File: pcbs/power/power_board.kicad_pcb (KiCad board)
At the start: 2 copper layers, 114 x 137.6 mm, 62 parts, among them J10 MR30PW-M, J11 MR30PW-M, J12 12V connection, J4 JST_XH_B3B, J5 JST_XH_B3B, J6 XT30PW-F, J7 XT30PW-F, J8 XT30PW-M, J9 MR30PW-M, U1 TPS5430DDA, U2 TPS5430DDA, U4 TPS5430DDA

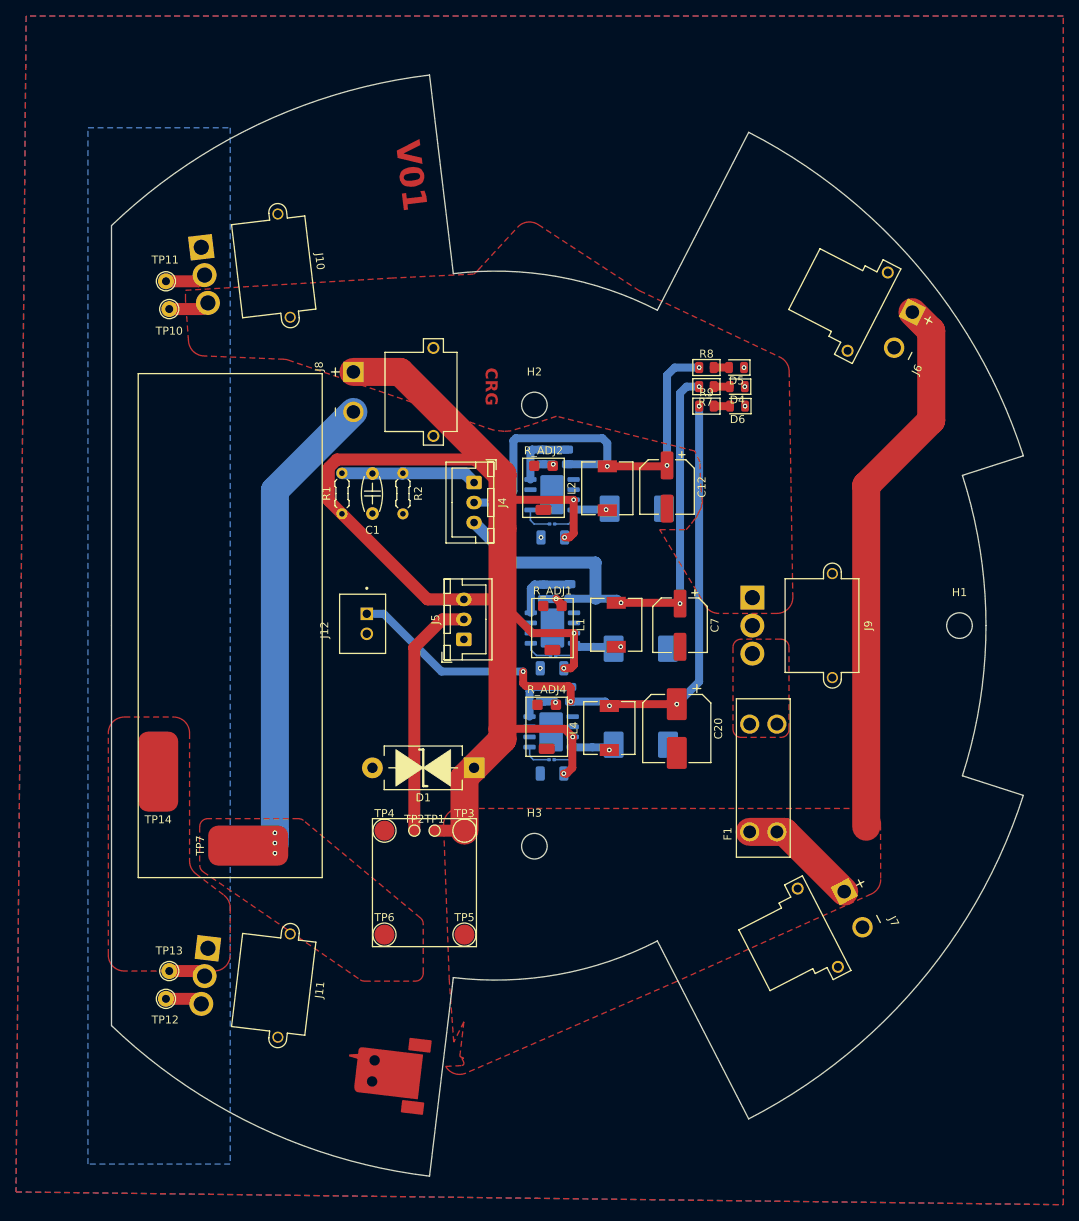
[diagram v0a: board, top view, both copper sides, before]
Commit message: Atualização para versão 10.0 do kicad Condensação do Layout Mudança no circuito V_mon para diminuir impedância de saída Implementação de Circuito "E-Switch" low side Resolução de EDR's no esquemático e PCB
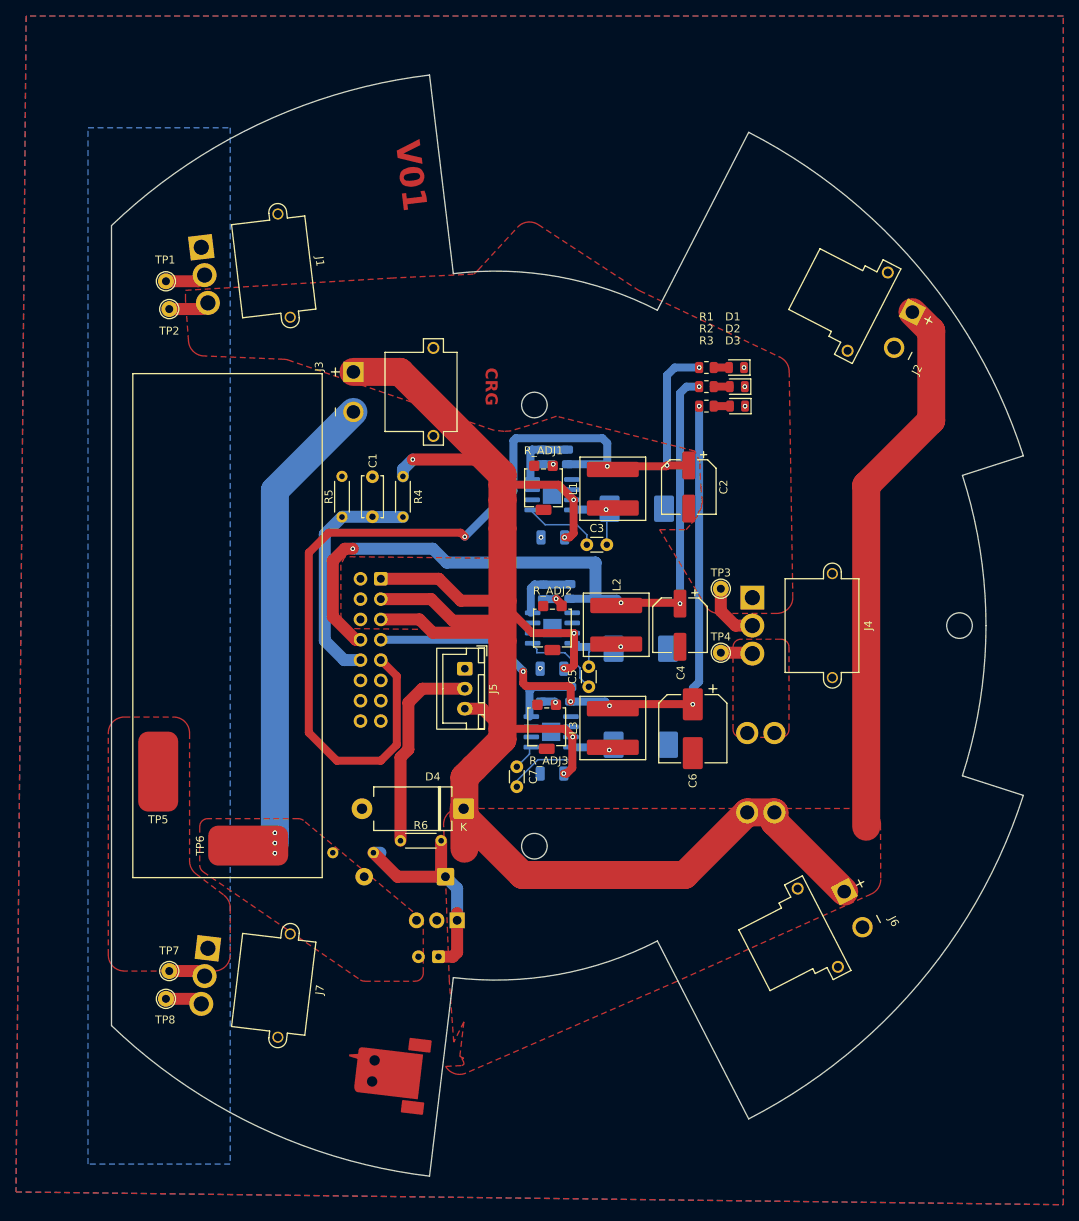
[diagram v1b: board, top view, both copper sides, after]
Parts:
- removed the C4 at (96.1, 91.4)
- removed the C6 at (96.2, 107.8)
- removed J12: 12V connection, oxebots_connectors:JST_B2B-XH-A
- removed the J4 at (86.3, 86.2)
- removed the TP1 at (81.4, 129.7)
- removed the TP2 at (78.8, 129.7)
- removed the TP5 at (85.1, 142.7)
- removed the TP6 at (75.1, 142.7)
- added C11: 10uF, Capacitor_THT:CP_Radial_D5.0mm_P2.50mm, B.Cu at (81.9, 145.5)
- added C3: 0.01uF, Capacitor_THT:C_Disc_D3.0mm_W1.6mm_P2.50mm, F.Cu at (100.4, 94.0)
- added C7: 0.01uF, Capacitor_THT:C_Disc_D3.0mm_W1.6mm_P2.50mm, F.Cu at (91.7, 121.7)
- added D8: 1N4744A, Diode_THT:D_DO-41_SOD81_P10.16mm_Horizontal, B.Cu at (82.7, 135.5)
- added J8: Conn_02x08_Odd_Even, Connector_IDC:IDC-Header_2x08_P2.54mm_Vertical, B.Cu at (74.7, 98.2)
- added Q1: IRFB3205, Package_TO_SOT_THT:TO-220-3_Vertical, B.Cu at (84.2, 140.9)
- added R13: 100K, Resistor_THT:R_Axial_DIN0204_L3.6mm_D1.6mm_P5.08mm_Horizontal, B.Cu at (73.7, 132.5)
- added R6: 10k, Resistor_THT:R_Axial_DIN0204_L3.6mm_D1.6mm_P5.08mm_Horizontal, F.Cu at (77.1, 131.0)
- C1: footprint PCM_Capacitor_THT_AKL:C_Disc_D5.0mm_W2.5mm_P5.00mm -> Capacitor_THT:C_Disc_D5.0mm_W2.5mm_P5.00mm
- C5: footprint Capacitor_SMD:C_0201_0603Metric -> Capacitor_THT:C_Disc_D3.0mm_W1.6mm_P2.50mm; moved to F.Cu
- D4: renamed from D1; footprint PCM_Diode_THT_AKL:D_DO-201_P12.70mm_Horizontal_TVS -> Diode_THT:D_DO-201_P12.70mm_Horizontal
- F1: value 30A -> 30; footprint oxebots:FUSE_3557-10 -> Fuse:Fuseholder_Blade_Mini_Keystone_3568; moved to B.Cu
- J1: renamed from J10; footprint oxebots_connectors:AMASS_MR30PW-M_1x03_P3.50mm_Horizontal -> oxebots:AMASS_MR30PW-M_1x03_P3.50mm_Horizontal
- J2: renamed from J6; footprint oxebots_connectors:AMASS_XT30PW-F -> oxebots:AMASS_XT30PW-F
- J3: renamed from J8; footprint oxebots_connectors:AMASS_XT30PW-M -> oxebots:AMASS_XT30PW-M
- J4: renamed from J9; footprint oxebots_connectors:AMASS_MR30PW-M_1x03_P3.50mm_Horizontal -> oxebots:AMASS_MR30PW-M_1x03_P3.50mm_Horizontal
- J6: renamed from J7; footprint oxebots_connectors:AMASS_XT30PW-F -> oxebots:AMASS_XT30PW-F
- J7: renamed from J11; footprint oxebots_connectors:AMASS_MR30PW-M_1x03_P3.50mm_Horizontal -> oxebots:AMASS_MR30PW-M_1x03_P3.50mm_Horizontal
- L1: renamed from L2; footprint Inductor_SMD:L_6.3x6.3_H3 -> Inductor_SMD:L_Coilcraft_XAL7070-XXX
- L2: renamed from L1; footprint Inductor_SMD:L_6.3x6.3_H3 -> Inductor_SMD:L_Coilcraft_XAL7070-XXX
- L3: renamed from L4; footprint Inductor_SMD:L_6.3x6.3_H3 -> Inductor_SMD:L_Coilcraft_XAL7070-XXX
- R1: renamed from R8; footprint PCM_Resistor_SMD_AKL:R_0805_2012Metric -> Resistor_SMD:R_0805_2012Metric
- R10: renamed from R4; footprint PCM_Resistor_SMD_AKL:R_0805_2012Metric -> Resistor_SMD:R_0805_2012Metric
- R11: renamed from R16; footprint PCM_Resistor_SMD_AKL:R_0805_2012Metric -> Resistor_SMD:R_0805_2012Metric
- R12: renamed from R15; footprint PCM_Resistor_SMD_AKL:R_0805_2012Metric -> Resistor_SMD:R_0805_2012Metric
- R2: renamed from R7; footprint PCM_Resistor_SMD_AKL:R_0805_2012Metric -> Resistor_SMD:R_0805_2012Metric
- R3: renamed from R9; footprint PCM_Resistor_SMD_AKL:R_0805_2012Metric -> Resistor_SMD:R_0805_2012Metric
- R4: renamed from R1; value 5.6M -> 56K; footprint PCM_Resistor_THT_AKL:R_Axial_DIN0204_L3.6mm_D1.6mm_P5.08mm_Horizontal -> Resistor_THT:R_Axial_DIN0204_L3.6mm_D1.6mm_P5.08mm_Horizontal
- R5: renamed from R2; value 220K -> 2.2K; footprint PCM_Resistor_THT_AKL:R_Axial_DIN0204_L3.6mm_D1.6mm_P5.08mm_Horizontal -> Resistor_THT:R_Axial_DIN0204_L3.6mm_D1.6mm_P5.08mm_Horizontal
- R7: renamed from R6; footprint PCM_Resistor_SMD_AKL:R_0805_2012Metric -> Resistor_SMD:R_0805_2012Metric
- R8: renamed from R5; footprint PCM_Resistor_SMD_AKL:R_0805_2012Metric -> Resistor_SMD:R_0805_2012Metric
- R9: renamed from R3; footprint PCM_Resistor_SMD_AKL:R_0805_2012Metric -> Resistor_SMD:R_0805_2012Metric
- R_ADJ1: renamed from R_ADJ2; footprint PCM_Potentiometer_SMD_AKL:Potentiometer_Bourns_3314G_Vertical -> Potentiometer_SMD:Potentiometer_Bourns_3314G_Vertical
- R_ADJ2: renamed from R_ADJ1; footprint PCM_Potentiometer_SMD_AKL:Potentiometer_Bourns_3314G_Vertical -> Potentiometer_SMD:Potentiometer_Bourns_3314G_Vertical
- R_ADJ3: renamed from R_ADJ4; footprint PCM_Potentiometer_SMD_AKL:Potentiometer_Bourns_3314G_Vertical -> Potentiometer_SMD:Potentiometer_Bourns_3314G_Vertical
- TP3: value V+ -> B5; footprint TestPoint:TestPoint_Pad_D2.5mm -> TestPoint:TestPoint_THTPad_D2.0mm_Drill1.0mm
- TP4: value V^{-}_{no} -> B6; footprint TestPoint:TestPoint_Pad_D2.5mm -> TestPoint:TestPoint_THTPad_D2.0mm_Drill1.0mm
- U1: renamed from U2; footprint PCM_Package_SO_AKL:Texas_HSOP-8-1EP_3.9x4.9mm_P1.27mm -> Package_SO:HSOP-8-1EP_3.9x4.9mm_P1.27mm_EP2.3x2.3mm
- U2: renamed from U1; footprint PCM_Package_SO_AKL:Texas_HSOP-8-1EP_3.9x4.9mm_P1.27mm -> Package_SO:HSOP-8-1EP_3.9x4.9mm_P1.27mm_EP2.3x2.3mm
- U3: renamed from U4; footprint PCM_Package_SO_AKL:Texas_HSOP-8-1EP_3.9x4.9mm_P1.27mm -> Package_SO:HSOP-8-1EP_3.9x4.9mm_P1.27mm_EP2.3x2.3mm
- moved TP4 47.6 mm to (117.2, 107.5)
- moved TP3 44.1 mm to (117.2, 99.5)
- moved C5 10.2 mm to (100.7, 111.7), turned to 90 degrees
- moved R5 9.39 mm to (69.8, 90.5), turned to 90 degrees
- moved R4 8.94 mm to (77.4, 85.4), turned to -90 degrees
- moved F1 5.97 mm to (120.5, 117.5), turned to -90 degrees
- moved D4 5.27 mm to (85.0, 127.0)
- moved C1 4.60 mm to (73.6, 85.5), turned to -90 degrees
- moved J5 3.67 mm to (85.2, 109.5), turned to -90 degrees
- moved C2 2.72 mm to (113.2, 86.8)
- moved C6 2.00 mm to (113.7, 117.0)
- moved L1 0.69 mm to (103.7, 87.0)
- moved L3 0.44 mm to (103.7, 116.9)
- moved C9 0.06 mm to (96.1, 109.5)
- renumbered C3 to C10, C12 to C2, C7 to C4, C20 to C6, C2 to C8, C8 to C9, D5 to D1, D4 to D2, D6 to D3, D2 to D5, D7 to D6, D3 to D7, H2 to H1, H1 to H2, TP11 to TP1, TP10 to TP2, TP14 to TP5, TP7 to TP6, TP13 to TP7, TP12 to TP8
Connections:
- net /V_{MON} renamed VMon
- C5 pad 1: Net-(D3-K) -> Net-(U1-BOOT)
- C5 pad 2: Net-(U4-BOOT) -> Net-(D7-K)
- J5 pad 2: Net-(J5-Pin_2) -> SW_{NO}
- TP3 pad 1: V_{ BATT} -> Net-(J9-Pin_2)
- TP4 pad 1: GND -> /B_{6s}
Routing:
- net +3.3V: track 55.1 -> 128.7 mm, vias 3 -> 4
- net V_{ BATT}: track 260.0 -> 319.7 mm, vias 6 -> 7
- net Net-(J5-Pin_2): track 30.5 -> 0.00 mm
- net Net-(D9-K): track 0.00 -> 29.8 mm
- net +5V: track 64.9 -> 93.5 mm, vias 3 -> 4
- net SW_{NO}: track 0.00 -> 25.4 mm
- net VMon: track 17.0 -> 29.4 mm
- net Net-(J9-Pin_2): track 0.00 -> 7.49 mm
- net Net-(U1-BOOT): track 3.58 -> 10.5 mm
- net Net-(D3-K): track 8.38 -> 14.9 mm
- net Net-(U2-BOOT): track 3.88 -> 9.58 mm
- net /B_{6s}: track 0.00 -> 3.99 mm
- net +12V: track 83.9 -> 82.0 mm
- net Net-(D7-K): track 9.75 -> 8.83 mm
- net Net-(D2-K): track 7.83 -> 8.73 mm
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
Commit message: Versão final com inclusão de test_points
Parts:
- added TP10: 5V, TestPoint:TestPoint_THTPad_D2.0mm_Drill1.0mm, F.Cu at (106.7, 80.0)
- added TP11: 3.3V, TestPoint:TestPoint_THTPad_D2.0mm_Drill1.0mm, F.Cu at (106.7, 74.5)
- added TP12: V_MON, TestPoint:TestPoint_THTPad_D2.0mm_Drill1.0mm, F.Cu at (82.7, 88.5)
- added TP13: V_BAT, TestPoint:TestPoint_THTPad_D2.0mm_Drill1.0mm, B.Cu at (135.2, 90.5)
- added TP9: 12V, TestPoint:TestPoint_THTPad_D2.0mm_Drill1.0mm, F.Cu at (118.2, 81.0)
- renumbered C7 to C10, C5 to C4, C3 to C5, C11 to C8, D8 to D3, H2 to H1, H1 to H2, J8 to J1, J1 to J5, J7 to J6, J5 to J7, R4 to R1, R5 to R2, R13 to R5, R6 to R8, TP8 to TP2, TP7 to TP3, TP5 to TP4, TP4 to TP5, TP3 to TP6, TP2 to TP7, TP1 to TP8
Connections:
- C8 pad 1: Net-(D9-K) -> Net-(D3-K)
- D3 pad 1: Net-(D9-K) -> Net-(D3-K)
- Q1 pad 1: Net-(D9-K) -> Net-(D3-K)
- R5 pad 1: Net-(D9-K) -> Net-(D3-K)
- R8 pad 2: Net-(D9-K) -> Net-(D3-K)
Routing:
- net Net-(D3-K): track 14.9 -> 58.3 mm
- net Net-(D9-K): track 29.8 -> 0.00 mm
- net VMon: track 29.4 -> 36.1 mm
- net +5V: track 93.5 -> 99.1 mm, vias 4 -> 5
- net +3.3V: track 128.7 -> 133.1 mm
- net +12V: track 82.0 -> 85.9 mm
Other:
- board text added: "12V"
- board text added: "3V3"
- board text added: "5V"

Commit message: DRC warnings solving
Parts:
- removed the C10 at (96.1, 122.6)
- removed the C4 at (112.1, 104.0)
- removed the C6 at (113.7, 117.0)
- removed the D1 at (119.1, 71.8)
- removed the J6 at (129.3, 141.9)
- removed the R1 at (115.4, 71.8)
- removed the R2 at (115.4, 74.2)
- removed the R3 at (115.4, 76.7)
- removed the TP6 at (58.1, 131.6)
- removed the TP6 at (117.2, 99.5)
- added C11: 220uF, Capacitor_SMD:CP_Elec_8x6.2, F.Cu at (113.7, 116.9)
- added C3: 100nF, Capacitor_THT:C_Disc_D3.0mm_W1.6mm_P2.50mm, F.Cu at (73.7, 90.5)
- added C7: 220uF, Capacitor_SMD:CP_Elec_6.3x7.7, F.Cu at (112.1, 104.0)
- added D8: B340, Diode_SMD:D_SMC, B.Cu at (107.2, 119.0)
- added R13: 10k, Resistor_SMD:R_0805_2012Metric, B.Cu at (98.2, 112.7)
- added R4: 2.7k, Resistor_SMD:R_0805_2012Metric, B.Cu at (95.0, 99.9)
- added R5: 5.6k, Resistor_SMD:R_0805_2012Metric, B.Cu at (95.2, 83.0)
- added TP15: P-, Connector_Wire:SolderWirePad_1x01_SMD_5x10mm, F.Cu at (57.9, 130.7)
- added TP6: B5, TestPoint:TestPoint_THTPad_D2.0mm_Drill1.0mm, F.Cu at (116.9, 98.2)
- C1: value 100nF -> 10uF; footprint Capacitor_THT:C_Disc_D5.0mm_W2.5mm_P5.00mm -> Capacitor_THT:CP_Radial_D5.0mm_P2.50mm
- C2: value 220uF -> 10uF; footprint Capacitor_SMD:CP_Elec_6.3x7.7 -> Capacitor_THT:CP_Radial_D5.0mm_P2.50mm
- C8: value 10uF -> 220uF; footprint Capacitor_SMD:C_1206_3216Metric -> Capacitor_SMD:CP_Elec_6.3x7.7; moved to F.Cu
- C9: footprint Capacitor_SMD:C_1206_3216Metric -> Capacitor_THT:CP_Radial_D5.0mm_P2.50mm; moved to F.Cu
- D2, D3: value LED -> B340; footprint LED_SMD:LED_0805_2012Metric -> Diode_SMD:D_SMC; moved to B.Cu
- D4: value 1.5KE30CA -> LED; footprint Diode_THT:D_DO-201_P12.70mm_Horizontal -> LED_SMD:LED_0805_2012Metric
- D5, D7: value B340 -> LED; footprint Diode_SMD:D_SMC -> LED_SMD:LED_0805_2012Metric; moved to F.Cu
- D6: value B340 -> 1.5KE30CA; footprint Diode_SMD:D_SMC -> Diode_THT:D_DO-201AE_P15.24mm_Horizontal; moved to F.Cu
- J2: value XT30PW-F -> XT30PW-M; footprint oxebots:AMASS_XT30PW-F -> oxebots:AMASS_XT30PW-M
- L1, L2, L3: footprint Inductor_SMD:L_Coilcraft_XAL7070-XXX -> Inductor_SMD:L_6.3x6.3_H3
- R10: value 2.7k -> 120; moved to F.Cu
- R11: value 10k -> 1k; moved to F.Cu
- R8: value 5.6k -> 10k
- R9: value 10k -> 330; moved to F.Cu
- R_ADJ1, R_ADJ2: value 1k -> 1K
- U1, U2, U3: footprint Package_SO:HSOP-8-1EP_3.9x4.9mm_P1.27mm_EP2.3x2.3mm -> Package_SO:TI_SO-PowerPAD-8_ThermalVias
- moved D4 63.0 mm to (119.4, 74.2)
- moved D7 43.9 mm to (119.2, 76.7), turned to 180 degrees
- moved R11 39.8 mm to (115.4, 76.7), turned to 0 degrees
- moved R10 34.8 mm to (115.4, 71.7), turned to 0 degrees
- moved D2 34.7 mm to (107.7, 107.0), turned to 0 degrees
- moved C2 32.5 mm to (90.7, 110.2), turned to 0 degrees
- moved R9 30.7 mm to (115.3, 74.2), turned to 0 degrees
- moved D6 29.7 mm to (85.0, 126.7), turned to 180 degrees
- moved C1 25.5 mm to (97.6, 94.0), turned to 180 degrees
- moved D5 21.7 mm to (119.2, 71.7), turned to 180 degrees
- moved D3 18.1 mm to (106.4, 89.5), turned to 0 degrees
- moved C8 18.1 mm to (113.2, 86.8), turned to -90 degrees
- moved R_ADJ2 17.6 mm to (95.0, 86.9)
- moved R_ADJ1 17.1 mm to (96.1, 104.0)
- moved L1 17.0 mm to (103.9, 104.0)
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- renumbered C8 to C4, C4 to C5, C5 to C6, D3 to D1, H3 to H2, H2 to H3, J7 to J4, J4 to J5, J5 to J6, J6 to J7, R5 to R1, R1 to R2, R2 to R3, R8 to R6
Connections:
- C1 pad 1: GND -> V_{ BATT}
- C1 pad 2: VMon -> GND
- C10 pad 2: Net-(D3-K) -> /Net-(D3-K)
- C2 pad 1: +3.3V -> V_{ BATT}
- C4 pad 1: Net-(D3-K) -> /Net-(D3-K)
- C5 pad 2: Net-(D7-K) -> /Net-(D7-K)
- C6 pad 2: Net-(D2-K) -> /Net-(D2-K)
- C8 pad 1: GND -> +3.3V
- C8 pad 2: V_{ BATT} -> GND
- C9 pad 1: GND -> V_{ BATT}
- C9 pad 2: V_{ BATT} -> GND
- D1 pad 1: Net-(D3-K) -> /Net-(D3-K)
- D2 pad 1: GND -> /Net-(D7-K)
- D2 pad 2: Net-(D4-A) -> GND
- D3 pad 1: GND -> /Net-(D2-K)
- D3 pad 2: Net-(D6-A) -> GND
- D4 pad 1: V_{ BATT} -> GND
- D4 pad 2: GND -> Net-(D4-A)
- D5 pad 1: Net-(D2-K) -> GND
- D5 pad 2: GND -> Net-(D5-A)
- D6 pad 1: Net-(D7-K) -> V_{ BATT}
- D7 pad 1: Net-(D3-K) -> GND
- D7 pad 2: GND -> Net-(D7-A)
- L1 pad 1: Net-(D2-K) -> /Net-(D7-K)
- L1 pad 2: +3.3V -> +5V
- L2 pad 1: Net-(D7-K) -> /Net-(D2-K)
- L2 pad 2: +5V -> +3.3V
- L3 pad 1: Net-(D3-K) -> /Net-(D3-K)
- Q1 pad 1: Net-(D3-K) -> /Net-(D3-K)
- R1 pad 1: Net-(D3-K) -> /Net-(D3-K)
- R10 pad 1: Net-(R4-Pad1) -> +3.3V
- R10 pad 2: Net-(U1-VSENSE) -> Net-(D5-A)
- R11 pad 2: Net-(U4-VSENSE) -> Net-(D7-A)
- R12 pad 2: Net-(U4-VSENSE) -> Net-(U3-VSENSE)
- R6 pad 2: Net-(D3-K) -> /Net-(D3-K)
- R7 pad 1: +3.3V -> +5V
- R7 pad 2: Net-(U2-VSENSE) -> Net-(U1-VSENSE)
- R8 pad 1: Net-(R5-Pad1) -> +3.3V
- R9 pad 2: Net-(U1-VSENSE) -> Net-(D4-A)
- R_ADJ1 pad 1: Net-(R5-Pad1) -> Net-(R4-Pad1)
- R_ADJ2 pad 1: Net-(R4-Pad1) -> Net-(R5-Pad1)
- U1 pad 1: Net-(U2-BOOT) -> Net-(U1-BOOT)
- U1 pad 4: Net-(U2-VSENSE) -> Net-(U1-VSENSE)
- U1 pad 8: Net-(D2-K) -> /Net-(D7-K)
- U2 pad 1: Net-(U1-BOOT) -> Net-(U2-BOOT)
- U2 pad 4: Net-(U1-VSENSE) -> Net-(U2-VSENSE)
- U2 pad 8: Net-(D7-K) -> /Net-(D2-K)
- U3 pad 4: Net-(U4-VSENSE) -> Net-(U3-VSENSE)
- U3 pad 8: Net-(D3-K) -> /Net-(D3-K)
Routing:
- net Net-(D3-K): track 58.3 -> 0.00 mm, vias 1 -> 0
- net /Net-(D3-K): track 0.00 -> 58.3 mm, vias 0 -> 1
- net V_{ BATT}: track 319.7 -> 307.9 mm, vias 7 -> 4
- net Net-(D7-K): track 8.83 -> 0.00 mm, vias 1 -> 0
- net /Net-(D7-K): track 0.00 -> 8.83 mm, vias 0 -> 1
- net Net-(D2-K): track 8.73 -> 0.00 mm, vias 1 -> 0
- net /Net-(D2-K): track 0.00 -> 8.73 mm, vias 0 -> 1
- net Net-(U3-VSENSE): track 0.00 -> 8.73 mm
- net Net-(U4-VSENSE): track 8.58 -> 0.00 mm
- net Net-(D7-A): track 0.00 -> 2.04 mm
- net Net-(D6-A): track 2.04 -> 0.00 mm
- net /Net-(J4-Pin_2): track 7.49 -> 8.84 mm
- net +12V: track 85.9 -> 85.0 mm
- net GND: vias 5 -> 3

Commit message: Board layout review and refresh fabrication outputs
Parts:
- removed J2: XT30PW-M, oxebots:AMASS_XT30PW-M
- D2, D3, D8, R12, R13, R4, R5, R7, R8, TP13, U1, U2, U3: moved to F.Cu
- F1: footprint Fuse:Fuseholder_Blade_Mini_Keystone_3568 -> Fuse:Fuse_Blade_Mini_directSolder
- moved TP2 106.7 mm to (62.4, 45.1), turned to 0 degrees
- moved TP3 102.1 mm to (59.2, 45.7), turned to 0 degrees
- moved TP5 77.4 mm to (75.1, 42.5)
- moved TP6 71.1 mm to (71.9, 43.2)
- moved TP11 43.8 mm to (150.0, 80.6)
- moved TP10 42.2 mm to (148.7, 77.5)
- moved D7 32.9 mm to (145.4, 96.5)
- moved D5 32.8 mm to (145.4, 91.4)
- moved R9 32.8 mm to (141.5, 94.0)
- moved D4 32.7 mm to (145.4, 94.0)
- moved R10 32.7 mm to (141.5, 91.5)
- moved R11 32.7 mm to (141.5, 96.5)
- moved TP9 30.1 mm to (147.5, 74.3)
- moved TP7 29.1 mm to (68.7, 43.8), turned to 0 degrees
- moved C2 24.7 mm to (102.0, 88.2)
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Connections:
- C10 pad 2: /Net-(D3-K) -> /SW_12V
- C4 pad 1: /Net-(D3-K) -> /Q1_GATE
- D1 pad 1: /Net-(D3-K) -> /Q1_GATE
- D8 pad 1: /Net-(D3-K) -> /SW_12V
- L3 pad 1: /Net-(D3-K) -> /SW_12V
- Q1 pad 1: /Net-(D3-K) -> /Q1_GATE
- R1 pad 1: /Net-(D3-K) -> /Q1_GATE
- R6 pad 2: /Net-(D3-K) -> /Q1_GATE
- U3 pad 8: /Net-(D3-K) -> /SW_12V
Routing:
- net /B_{6s}: track 3.99 -> 158.3 mm
- net /Net-(J4-Pin_2): track 8.84 -> 142.4 mm
- net /Net-(J6-Pin_2): track 4.68 -> 136.1 mm, vias 0 -> 1
- net +5V: track 99.1 -> 188.0 mm, vias 5 -> 4
- net V_{ BATT}: track 307.9 -> 220.6 mm, vias 4 -> 15
- net +12V: track 85.0 -> 154.0 mm
- net /Net-(D3-K): track 58.3 -> 0.00 mm, vias 1 -> 0
- net GND_{BMS}: track 58.0 -> 0.00 mm, vias 3 -> 10
- net /SW_12V: track 0.00 -> 31.2 mm
- net /Q1_GATE: track 0.00 -> 28.0 mm
- net /B_{4s}: track 5.15 -> 26.5 mm, vias 0 -> 13
- net /Net-(D7-K): track 8.83 -> 29.2 mm
- net /Net-(J5-Pin_2): track 5.15 -> 21.5 mm
- net /Net-(D2-K): track 8.73 -> 24.6 mm
- net +3.3V: track 133.1 -> 146.8 mm
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- added copper zone on B.Cu, net /B_{4s}
- added copper zone on B.Cu, net GND_{BMS}
- added copper zone on B.Cu, net V_{ BATT}
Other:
- board text added: "B1"
- board text added: "B2"
- board text added: "B3"
- board text added: "B4"
- board text added: "B5"
- board text added: "B6"
- board text added: "BAT 2S2P"
- board text added: "BAT 4S2P"
- board text added: "BAT 6S2P"
- board text added: "GND"
- board text added: "Notes:"
- board text added: "V_{BAT}"
- board text added: "~24V"
- board text removed: "V01"
